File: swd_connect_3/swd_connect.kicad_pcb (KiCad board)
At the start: 2 copper layers, 38 x 19 mm, 2 parts, among them J1 Link-E Receptacle, J2 swd-connect-3

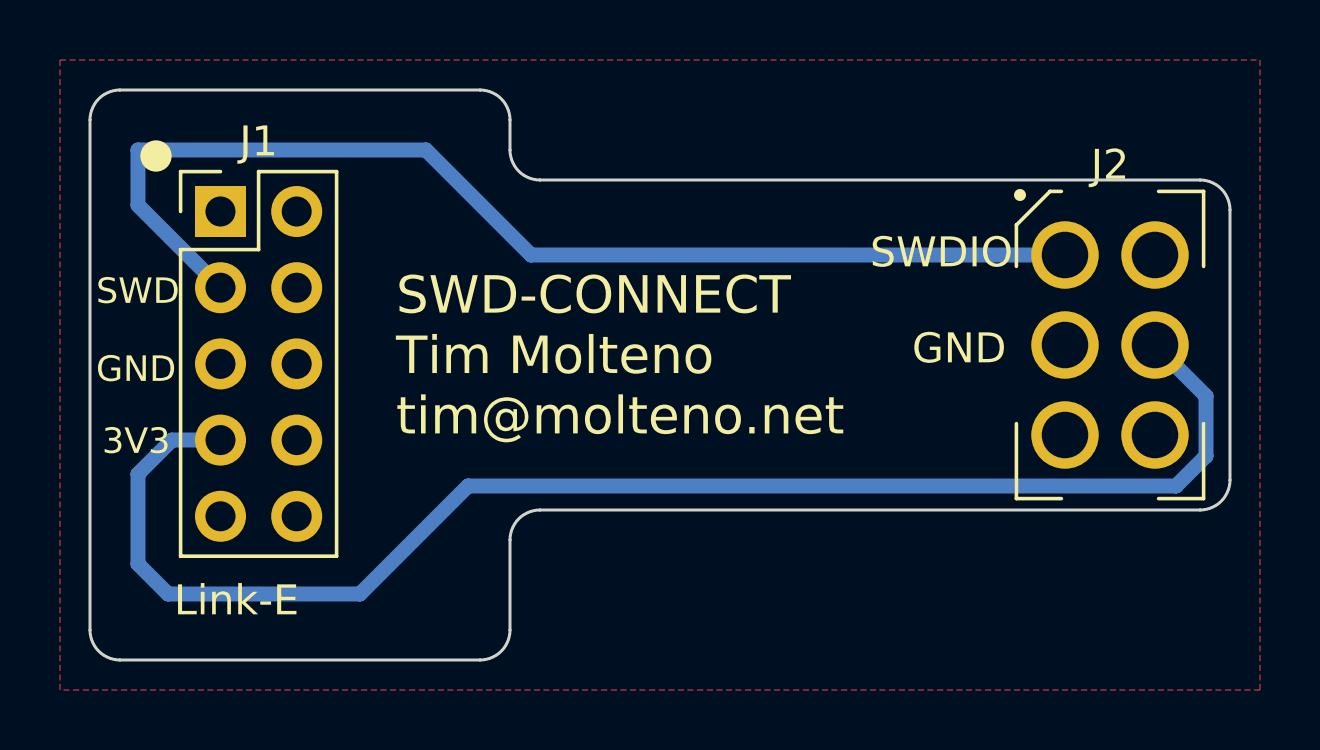
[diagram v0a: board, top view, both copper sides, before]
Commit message: Make all holes the same size. Add tight version of the -3 connector
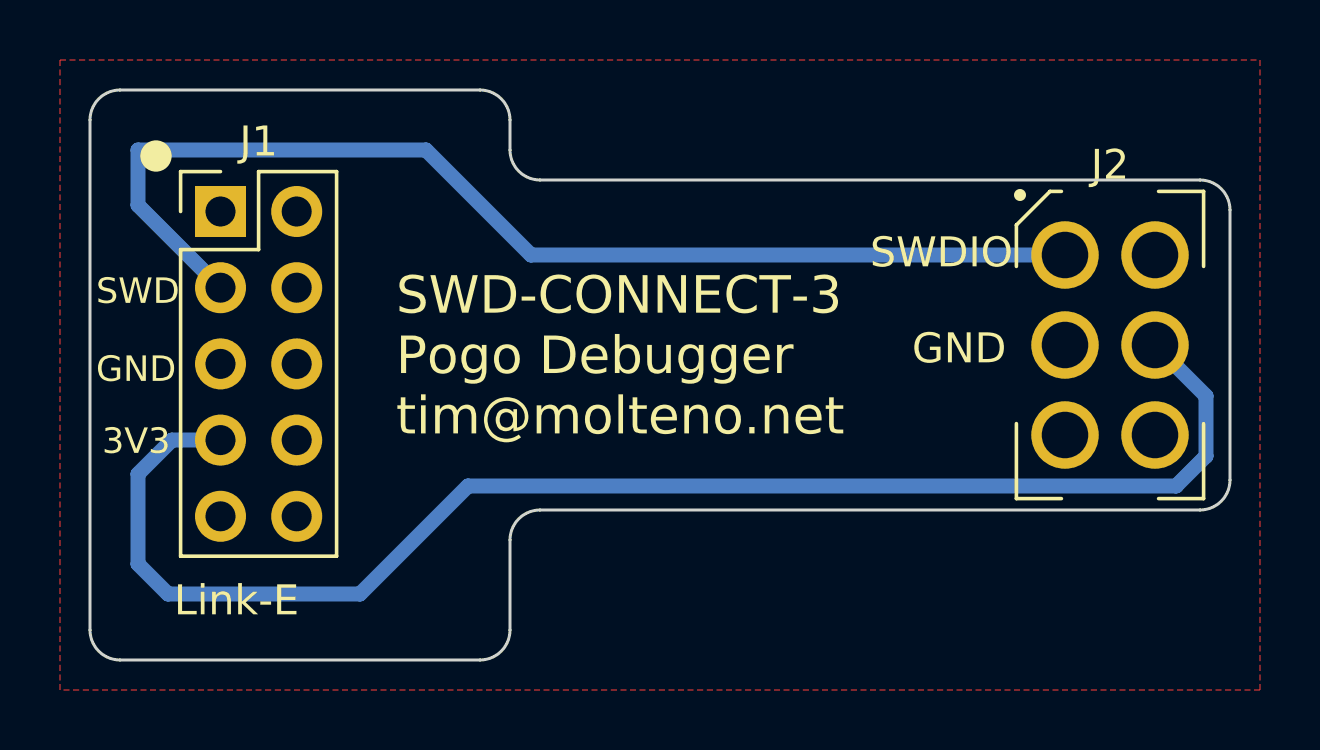
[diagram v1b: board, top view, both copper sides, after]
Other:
- board text added: "SWD-CONNECT-3 Pogo Debugger tim@molteno.net"
- board text removed: "SWD-CONNECT Tim Molteno tim@molteno.net"
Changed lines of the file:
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@@
     (effects (font (size 1 1) (thickness 0.15)) (justify left bottom))
   )
-  (gr_text "SWD-CONNECT\nTim Molteno\ntim@molteno.net" (at 164.2 63.6) (layer "F.SilkS")
+  (gr_text "SWD-CONNECT-3\nPogo Debugger\ntim@molteno.net" (at 164.2 63.6) (layer "F.SilkS")
     (effects (font (size 1.25 1.25) (thickness 0.2)) (justify left bottom))
   )

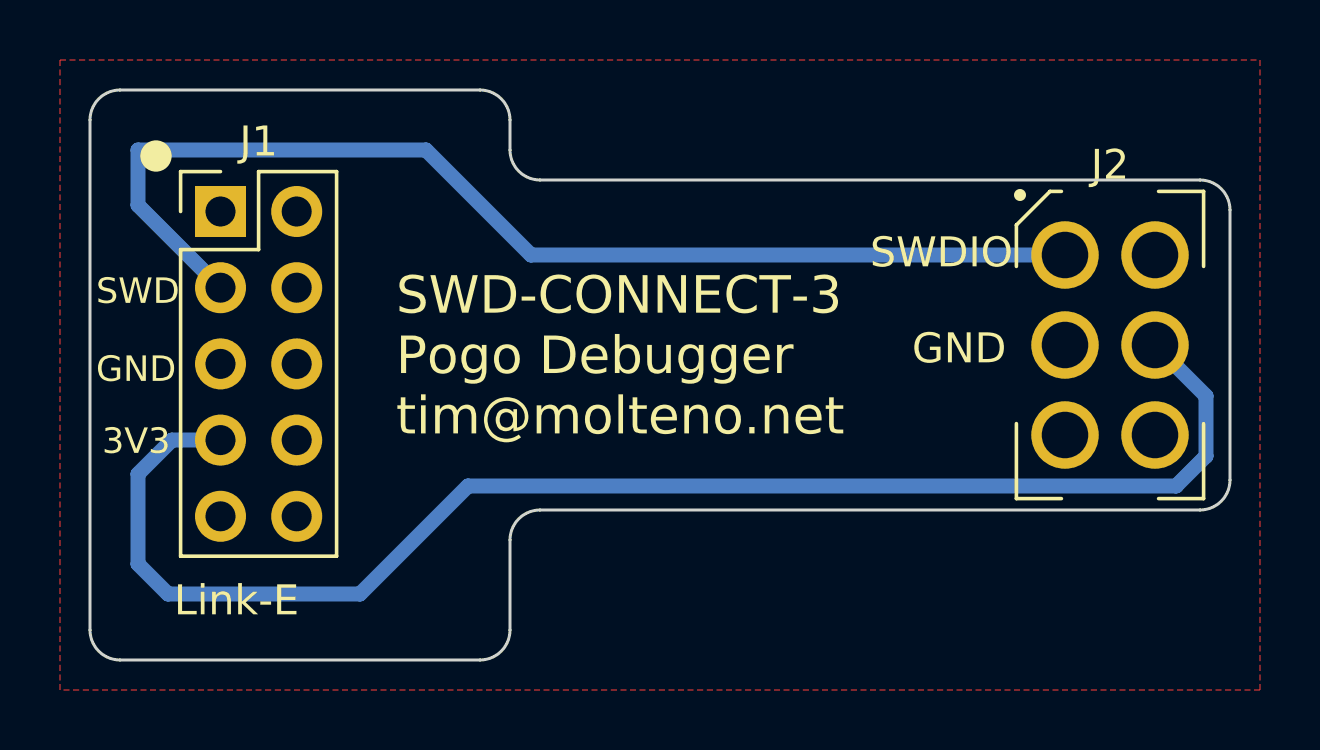
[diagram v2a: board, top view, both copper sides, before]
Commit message: Update symbol to reflect the actual layout
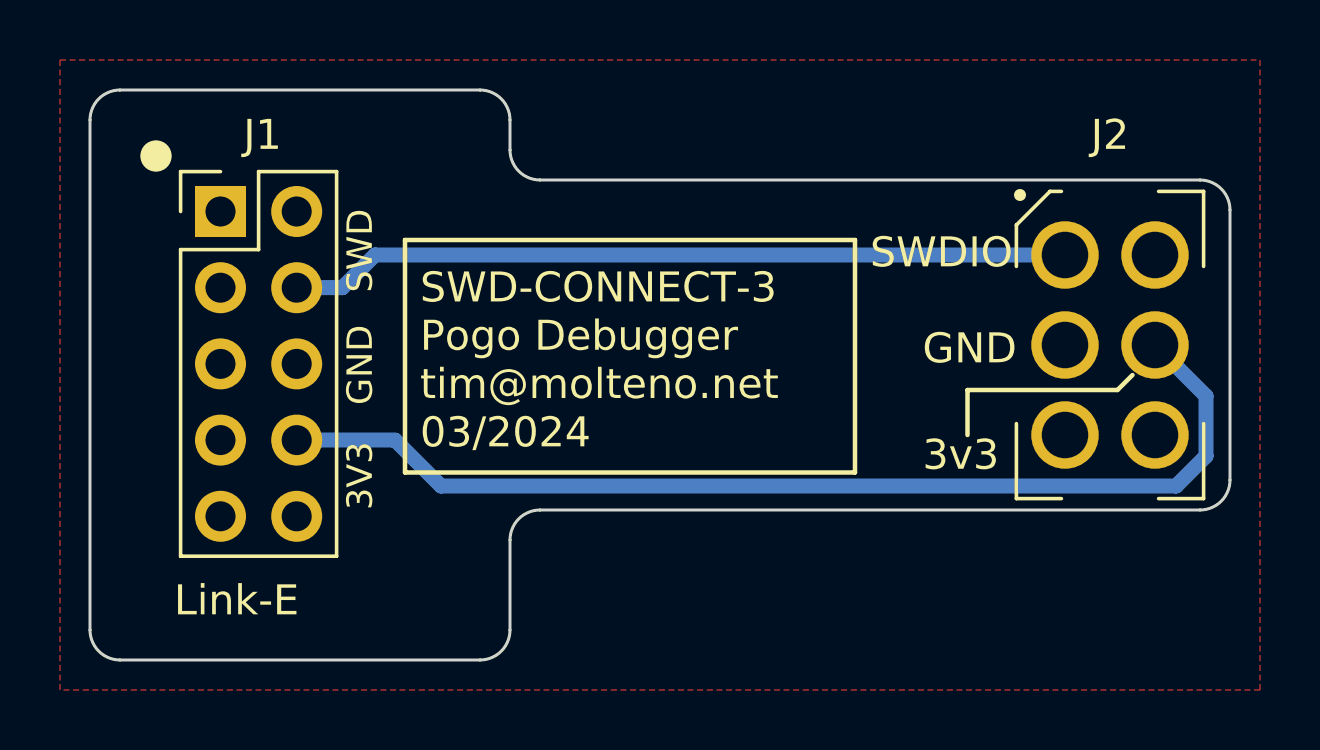
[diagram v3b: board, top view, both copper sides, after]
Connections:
- J1 pad 3: Net-(J1-SWDIO) -> unconnected-(J1-TX-Pad3)
- J1 pad 4: unconnected-(J1-TX-Pad4) -> Net-(J1-SWDIO)
- J1 pad 5: GND -> unconnected-(J1-TD0-Pad5)
- J1 pad 7: Net-(J2-3V3) -> unconnected-(J1-TDI-Pad7)
- J1 pad 8: unconnected-(J1-3V3-Pad8) -> Net-(J1-3V3)
- J2 pad 3: Net-(J2-3V3) -> Net-(J1-3V3)
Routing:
- net Net-(J2-3V3): track 48.5 -> 0.00 mm
- net Net-(J1-3V3): track 0.00 -> 35.8 mm
- net Net-(J1-SWDIO): track 38.1 -> 26.1 mm
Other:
- board text added: "3v3"
- board text added: "SWD-CONNECT-3 Pogo Debugger tim@molteno.net 03/2024"
- board text removed: "SWD-CONNECT-3 Pogo Debugger tim@molteno.net"
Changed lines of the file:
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@@
   )
   (net 0 "")
-  (net 1 "unconnected-(J1-SWCLK-Pad1)")
+  (net 1 "unconnected-(J1-RX-Pad1)")
   (net 2 "GND")
-  (net 3 "Net-(J2-3V3)")
-  (net 4 "unconnected-(J1-RX-Pad2)")
-  (net 5 "unconnected-(J1-TX-Pad4)")
-  (net 6 "unconnected-(J1-3V3-Pad8)")
-  (net 7 "unconnected-(J1-5V-Pad9)")
-  (net 8 "unconnected-(J1-RST-Pad10)")
+  (net 3 "unconnected-(J1-SWCLK-Pad2)")
+  (net 4 "unconnected-(J1-TX-Pad3)")
+  (net 5 "unconnected-(J1-TD0-Pad5)")
+  (net 6 "unconnected-(J1-TDI-Pad7)")
+  (net 7 "Net-(J1-3V3)")
+  (net 8 "unconnected-(J1-RST-Pad9)")
   (net 9 "Net-(J1-SWDIO)")
+  (net 10 "unconnected-(J1-5V-Pad10)")
   (footprint "swd-connect:swd-connect-3-programmer" (layer "F.Cu")
     (at 188 60.5)
@@
     (property "exclude_from_bom" "")
     (property "ki_description" "Simple SWD programming footprint (MCU side)")
-    (attr smd)
-    (fp_text reference "J2" (at 0 -6) (layer "F.SilkS")
+    (attr smd exclude_from_bom)
+    (fp_text reference "J2" (at 0 -7) (layer "F.SilkS")
         (effects (font (size 1 1) (thickness 0.15)))
     )
@@
       (net 2 "GND") (pinfunction "GND") (pintype "unspecified"))
     (pad "3" thru_hole circle (at 1.5 0) (size 2.25 2.25) (drill 1.55) (layers "*.Cu" "*.Mask")
-      (net 3 "Net-(J2-3V3)") (pinfunction "3V3") (pintype "unspecified"))
+      (net 7 "Net-(J1-3V3)") (pinfunction "3V3") (pintype "unspecified"))
   )
   (footprint "Connector_PinHeader_2.54mm:PinHeader_2x05_P2.54mm_Vertical" (layer "F.Cu")
@@
     (property "ki_description" "Link_E  connector for programming WCH chips including ch32v series using SWD.")
     (attr through_hole)
-    (fp_text reference "J1" (at 1.27 -2.33) (layer "F.SilkS")
+    (fp_text reference "J1" (at 1.4 -2.55) (layer "F.SilkS")
         (effects (font (size 1 1) (thickness 0.15)))
     )
@@
         (effects (font (size 1 1) (thickness 0.15)))
     )
-    (fp_text user "${REFERENCE}" (at 1.27 5.08 90) (layer "F.Fab")
+    (fp_text user "${REFERENCE}" (at -2.85 4.45 90) (layer "F.Fab")
         (effects (font (size 1 1) (thickness 0.15)))
     )
@@
       (stroke (width 0.1) (type solid)) (layer "F.Fab"))
     (pad "1" thru_hole rect (at 0 0) (size 1.7 1.7) (drill 1) (layers "*.Cu" "*.Mask")
-      (net 1 "unconnected-(J1-SWCLK-Pad1)") (pinfunction "SWCLK") (pintype "unspecified"))
+      (net 1 "unconnected-(J1-RX-Pad1)") (pinfunction "RX") (pintype "unspecified"))
     (pad "2" thru_hole oval (at 2.54 0) (size 1.7 1.7) (drill 1) (layers "*.Cu" "*.Mask")
-      (net 4 "unconnected-(J1-RX-Pad2)") (pinfunction "RX") (pintype "unspecified"))
+      (net 3 "unconnected-(J1-SWCLK-Pad2)") (pinfunction "SWCLK") (pintype "unspecified"))
     (pad "3" thru_hole oval (at 0 2.54) (size 1.7 1.7) (drill 1) (layers "*.Cu" "*.Mask")
+      (net 4 "unconnected-(J1-TX-Pad3)") (pinfunction "TX") (pintype "unspecified"))
+    (pad "4" thru_hole oval (at 2.54 2.54) (size 1.7 1.7) (drill 1) (layers "*.Cu" "*.Mask")
       (net 9 "Net-(J1-SWDIO)") (pinfunction "SWDIO") (pintype "unspecified"))
-    (pad "4" thru_hole oval (at 2.54 2.54) (size 1.7 1.7) (drill 1) (layers "*.Cu" "*.Mask")
-      (net 5 "unconnected-(J1-TX-Pad4)") (pinfunction "TX") (pintype "unspecified"))
     (pad "5" thru_hole oval (at 0 5.08) (size 1.7 1.7) (drill 1) (layers "*.Cu" "*.Mask")
-      (net 2 "GND") (pinfunction "GND") (pintype "unspecified"))
+      (net 5 "unconnected-(J1-TD0-Pad5)") (pinfunction "TD0") (pintype "unspecified"))
     (pad "6" thru_hole oval (at 2.54 5.08) (size 1.7 1.7) (drill 1) (layers "*.Cu" "*.Mask")
       (net 2 "GND") (pinfunction "GND") (pintype "unspecified"))
     (pad "7" thru_hole oval (at 0 7.62) (size 1.7 1.7) (drill 1) (layers "*.Cu" "*.Mask")
-      (net 3 "Net-(J2-3V3)") (pinfunction "3V3") (pintype "unspecified"))
+      (net 6 "unconnected-(J1-TDI-Pad7)") (pinfunction "TDI") (pintype "unspecified"))
     (pad "8" thru_hole oval (at 2.54 7.62) (size 1.7 1.7) (drill 1) (layers "*.Cu" "*.Mask")
-      (net 6 "unconnected-(J1-3V3-Pad8)") (pinfunction "3V3") (pintype "unspecified"))
+      (net 7 "Net-(J1-3V3)") (pinfunction "3V3") (pintype "unspecified"))
     (pad "9" thru_hole oval (at 0 10.16) (size 1.7 1.7) (drill 1) (layers "*.Cu" "*.Mask")
-      (net 7 "unconnected-(J1-5V-Pad9)") (pinfunction "5V") (pintype "unspecified"))
+      (net 8 "unconnected-(J1-RST-Pad9)") (pinfunction "RST") (pintype "unspecified"))
     (pad "10" thru_hole oval (at 2.54 10.16) (size 1.7 1.7) (drill 1) (layers "*.Cu" "*.Mask")
-      (net 8 "unconnected-(J1-RST-Pad10)") (pinfunction "RST") (pintype "unspecified"))
+      (net 10 "unconnected-(J1-5V-Pad10)") (pinfunction "5V") (pintype "unspecified"))
     (model "${KICAD6_3DMODEL_DIR}/Connector_PinHeader_2.54mm.3dshapes/PinHeader_2x05_P2.54mm_Vertical.wrl"
       (offset (xyz 0 0 0))
@@
     )
   )
+  (gr_line (start 183.25 62) (end 183.25 63.5)
+    (stroke (width 0.15) (type default)) (layer "F.SilkS"))
+  (gr_rect (start 164.5 57) (end 179.5 64.75)
+    (stroke (width 0.15) (type default)) (fill none) (layer "F.SilkS"))
   (gr_circle (center 156.2 54.2) (end 156.647214 54.2)
     (stroke (width 0.15) (type solid)) (fill solid) (layer "F.SilkS"))
+  (gr_line (start 183.25 62) (end 188.25 62)
+    (stroke (width 0.15) (type default)) (layer "F.SilkS"))
+  (gr_line (start 188.25 62) (end 188.75 61.5)
+    (stroke (width 0.15) (type default)) (layer "F.SilkS"))
   (gr_arc (start 167 52) (mid 167.707107 52.292893) (end 168 53)
     (stroke (width 0.1) (type default)) (layer "Edge.Cuts"))
@@
   (gr_arc (start 192 65) (mid 191.707107 65.707107) (end 191 66)
     (stroke (width 0.1) (type default)) (layer "Edge.Cuts"))
+  (gr_text "SWD-CONNECT-3\nPogo Debugger\ntim@molteno.net\n03/2024" (at 166.75 64.25) (layer "B.SilkS")
+    (effects (font (size 1 1) (thickness 0.2)) (justify left bottom))
+  )
   (gr_text "SWDIO" (at 180 58) (layer "F.SilkS")
     (effects (font (size 1 1) (thickness 0.15)) (justify left bottom))
   )
-  (gr_text "SWD" (at 154.2 59.2) (layer "F.SilkS")
+  (gr_text "3v3" (at 181.75 64.748996) (layer "F.SilkS")
+    (effects (font (size 1 1) (thickness 0.15)) (justify left bottom))
+  )
+  (gr_text "SWD" (at 163.5 58.75 90) (layer "F.SilkS")
     (effects (font (size 0.85 0.85) (thickness 0.15)) (justify left bottom))
   )
-  (gr_text "3V3" (at 154.4 64.2) (layer "F.SilkS")
+  (gr_text "3V3" (at 163.5 66 90) (layer "F.SilkS")
     (effects (font (size 0.85 0.85) (thickness 0.15)) (justify left bottom))
   )
-  (gr_text "GND" (at 181.4 61.2) (layer "F.SilkS")
-    (effects (font (size 1 1) (thickness 0.15)) (justify left bottom))
-  )
-  (gr_text "GND" (at 154.2 61.8) (layer "F.SilkS")
+  (gr_text "GND" (at 181.75 61.2) (layer "F.SilkS")
+    (effects (font (size 1 1) (thickness 0.15)) (justify left bottom))
+  )
+  (gr_text "GND" (at 163.5 62.5 90) (layer "F.SilkS")
     (effects (font (size 0.85 0.85) (thickness 0.15)) (justify left bottom))
   )
@@
     (effects (font (size 1 1) (thickness 0.15)) (justify left bottom))
   )
-  (gr_text "SWD-CONNECT-3\nPogo Debugger\ntim@molteno.net" (at 164.2 63.6) (layer "F.SilkS")
-    (effects (font (size 1.25 1.25) (thickness 0.2)) (justify left bottom))
-  )
-  (segment (start 156.6 68.8) (end 163 68.8) (width 0.5) (layer "B.Cu") (net 3))
-  (segment (start 190.204164 65.2) (end 191.2 64.204164) (width 0.5) (layer "B.Cu") (net 3))
-  (segment (start 155.6 64.8) (end 155.6 67.8) (width 0.5) (layer "B.Cu") (net 3))
-  (segment (start 158.35 63.67) (end 156.73 63.67) (width 0.5) (layer "B.Cu") (net 3))
-  (segment (start 163 68.8) (end 166.6 65.2) (width 0.5) (layer "B.Cu") (net 3))
-  (segment (start 191.2 64.204164) (end 191.2 62.2) (width 0.5) (layer "B.Cu") (net 3))
-  (segment (start 156.73 63.67) (end 155.6 64.8) (width 0.5) (layer "B.Cu") (net 3))
-  (segment (start 166.6 65.2) (end 190.204164 65.2) (width 0.5) (layer "B.Cu") (net 3))
-  (segment (start 155.6 67.8) (end 156.6 68.8) (width 0.5) (layer "B.Cu") (net 3))
-  (segment (start 191.2 62.2) (end 189.5 60.5) (width 0.5) (layer "B.Cu") (net 3))
-  (segment (start 155.6 54) (end 165.2 54) (width 0.5) (layer "B.Cu") (net 9))
-  (segment (start 155.6 55.84) (end 155.6 54) (width 0.5) (layer "B.Cu") (net 9))
-  (segment (start 168.7 57.5) (end 186.5 57.5) (width 0.5) (layer "B.Cu") (net 9))
-  (segment (start 158.35 58.59) (end 155.6 55.84) (width 0.5) (layer "B.Cu") (net 9))
-  (segment (start 165.2 54) (end 168.7 57.5) (width 0.5) (layer "B.Cu") (net 9))
+  (gr_text "SWD-CONNECT-3\nPogo Debugger\ntim@molteno.net\n03/2024" (at 165 64) (layer "F.SilkS")
+    (effects (font (size 1 1) (thickness 0.2)) (justify left bottom))
+  )
+  (segment (start 191.2 64.204164) (end 190.204164 65.2) (width 0.5) (layer "B.Cu") (net 7))
+  (segment (start 164.17 63.67) (end 160.89 63.67) (width 0.5) (layer "B.Cu") (net 7))
+  (segment (start 189.5 60.5) (end 191.2 62.2) (width 0.5) (layer "B.Cu") (net 7))
+  (segment (start 190.204164 65.2) (end 165.7 65.2) (width 0.5) (layer "B.Cu") (net 7))
+  (segment (start 165.7 65.2) (end 164.17 63.67) (width 0.5) (layer "B.Cu") (net 7))
+  (segment (start 191.2 62.2) (end 191.2 64.204164) (width 0.5) (layer "B.Cu") (net 7))
+  (segment (start 163.5 57.5) (end 162.41 58.59) (width 0.5) (layer "B.Cu") (net 9))
+  (segment (start 162.41 58.59) (end 160.89 58.59) (width 0.5) (layer "B.Cu") (net 9))
+  (segment (start 186.5 57.5) (end 163.5 57.5) (width 0.5) (layer "B.Cu") (net 9))
   (zone (net 2) (net_name "GND") (layer "F.Cu") (hatch edge 0.5)
     (connect_pads (clearance 0.2))

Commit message: Updated swd connect
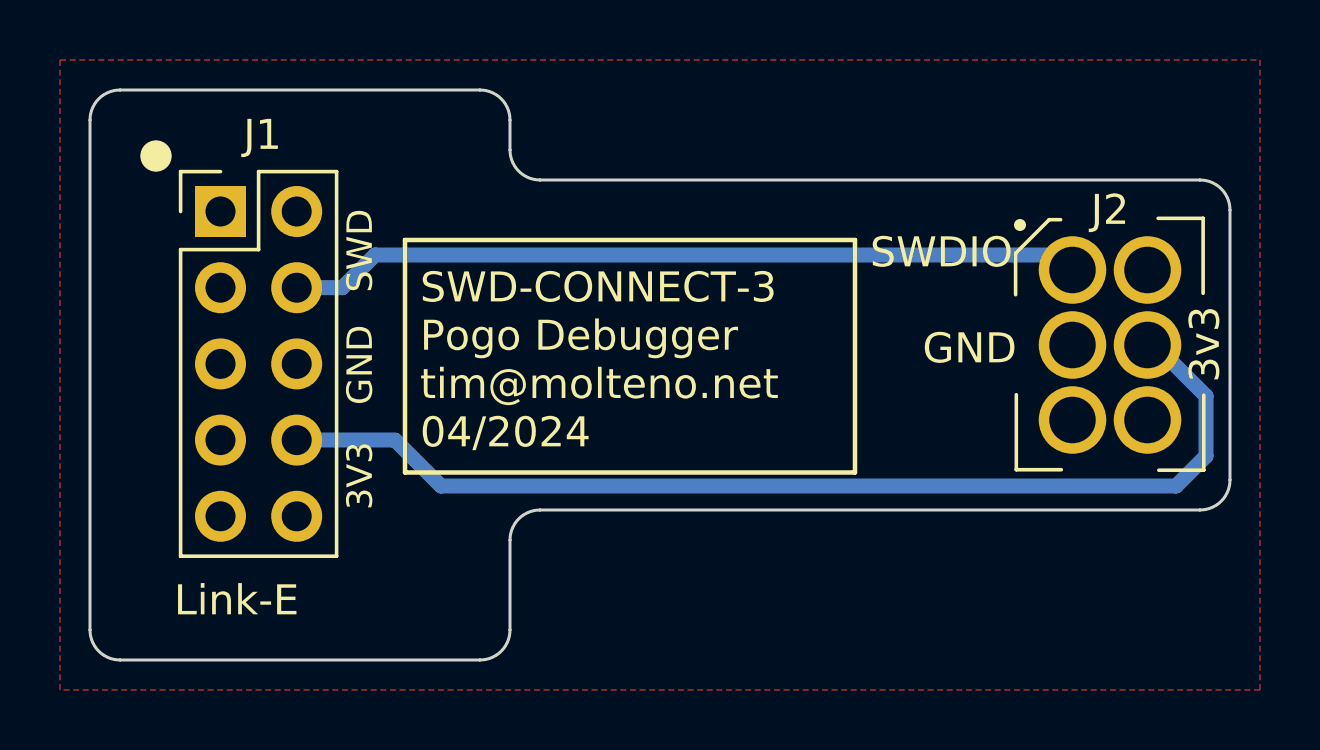
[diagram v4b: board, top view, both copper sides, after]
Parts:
- J2: footprint swd-connect:swd-connect-3-programmer -> swd-connect:swd-connect-3-programmer-tight
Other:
- board text added: "SWD-CONNECT-3 Pogo Debugger tim@molteno.net 04/2024"
- board text removed: "SWD-CONNECT-3 Pogo Debugger tim@molteno.net 03/2024"
